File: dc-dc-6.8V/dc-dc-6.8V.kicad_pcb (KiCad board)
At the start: 2 copper layers, 32 x 37 mm, 23 parts, among them P1 1.8mm_16AWG, P2 1.8mm_16AWG, P3 1.8mm_16AWG, P4 1.8mm_16AWG, Q3 DOD4185, U2 LM25085MY/NOPB

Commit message: update
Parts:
- removed C10: 1nF, bio-robot:C_0603_1608Metric
- removed C11: 3.3nF, bio-robot:C_0603_1608Metric
- removed C12: 47uF, bio-robot:CAP_EEEFT1H470AP
- removed D2: STPS20M100SG-TR, bio-robot:TO-263-2
- removed H5, H6, H7, H8: MountingHoleM3, MountingHole:MountingHole_3.2mm_M3_DIN965_Pad
- removed L2: 3.3uH, bio-robot:IND_MDA1050-3R3M
- removed Q3: DOD4185, bio-robot:DPAK-3_ONS
- removed R5: 10m, bio-robot:R_0805_2012Metric
- removed R8: 10k, bio-robot:R_0603_1608Metric
- removed R9: 2.26k, bio-robot:R_0603_1608Metric
- removed U2: LM25085MY/NOPB, bio-robot:MSOP8_PowerPad
- added C1: 22u_1206, bots:C_1206_3216Metric, F.Cu at (117.2, 71.2)
- added C2: 22u_1206, bots:C_1206_3216Metric, F.Cu at (114.8, 71.2)
- added C3: 22u_1206, bots:C_1206_3216Metric, F.Cu at (112.2, 71.2)
- added C4: 0.1u, bots:C_0603_1608Metric, F.Cu at (119.2, 72.0)
- added C5: 15nF, bio-robot:C_0603_1608Metric, F.Cu at (149.2, 123.6)
- added C6: 0.47u, bio-robot:C_0603_1608Metric, F.Cu at (152.5, 118.2)
- added H1: MountingHoleM3, bio-robot:MountingHole_3.2mm_M3_DIN965_Pad, F.Cu at (109.5, 60.0)
- added H2: MountingHoleM3, bio-robot:MountingHole_3.2mm_M3_DIN965_Pad, F.Cu at (139.5, 60.0)
- added H3: MountingHoleM3, bio-robot:MountingHole_3.2mm_M3_DIN965_Pad, F.Cu at (109.5, 85.0)
- added H4: MountingHoleM3, bio-robot:MountingHole_3.2mm_M3_DIN965_Pad, F.Cu at (139.5, 85.0)
- added L1: 1.8uH, bio-robot:IND_XAL7070_COC, F.Cu at (131.0, 100.0)
- added Q1: SVD5865NLT4G, bots:DPAK-3_ONS, F.Cu at (127.8, 110.9)
- added Q2: SVD5865NLT4G, bots:DPAK-3_ONS, F.Cu at (136.7, 110.9)
- added R1: 137k, bio-robot:R_0603_1608Metric, F.Cu at (121.2, 104.6)
- added R2: 806R, bots:R_0603_1608Metric, F.Cu at (121.2, 107.1)
- added U1: LM3150MHX_NOPB, bio-robot:SOP65P640X110-15N, F.Cu at (124.8, 74.5)
- C7: value 22u_1206 -> 2.2u; footprint bots:C_1206_3216Metric -> bio-robot:C_0603_1608Metric
- C8: value 22u_1206 -> 180pF; footprint bots:C_1206_3216Metric -> bio-robot:C_0603_1608Metric
- C9: value 0.47u -> 82uF; footprint bio-robot:C_0603_1608Metric -> bio-robot:CAP_10SVPC120MV
- R3: value 113k -> 9.76k; footprint bio-robot:R_0603_1608Metric -> bots:R_0603_1608Metric; moved to F.Cu
- R4: value 4.12k -> 102k; footprint bio-robot:R_0603_1608Metric -> bots:R_0603_1608Metric; moved to F.Cu
- moved R4 62.9 mm to (168.8, 109.2), turned to 0 degrees
- moved R3 57.8 mm to (149.2, 126.1), turned to 0 degrees
- moved P3 37.5 mm to (156.2, 63.2), turned to 90 degrees
- moved P4 37.2 mm to (154.0, 74.5), turned to 0 degrees
- moved C9 24.8 mm to (99.8, 90.8)
- moved C8 18.5 mm to (112.2, 94.1), turned to 0 degrees
- moved P1 17.3 mm to (95.2, 68.0), turned to 90 degrees
- moved P2 15.1 mm to (98.0, 76.5), turned to 180 degrees
- moved C7 9.39 mm to (122.5, 71.0), turned to 0 degrees
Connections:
- C7 pad 1: VCC -> /CVCC
- C8 pad 1: VCC -> +6.8V
- C8 pad 2: GND -> /FB
- C9 pad 1: VCC -> +6.8V
- C9 pad 2: /CVCC -> GND
- R3 pad 1: VCC -> /FB
- R3 pad 2: /RT -> GND
- R4 pad 1: /ADJ -> +6.8V
- R4 pad 2: VCC -> /FB
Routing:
- net /FB1: track 6.86 -> 0.00 mm
- net /ADJ: track 4.73 -> 0.00 mm, vias 1 -> 0
- net /RT: track 4.29 -> 0.00 mm, vias 1 -> 0
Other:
- board size 32 x 37 mm -> 37 x 32 mm

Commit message: update
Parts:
- C1, C2, C3: footprint bots:C_1206_3216Metric -> bio-robot:C_1206_3216Metric
- Q1, Q2: footprint bots:DPAK-3_ONS -> bio-robot:SOIC-8_3.9x4.9mm_P1.27mm
- moved C6 51.1 mm to (129.3, 72.8), turned to 180 degrees
- moved Q1 46.9 mm to (124.0, 64.2), turned to 180 degrees
- moved C5 46.5 mm to (126.0, 83.2), turned to 180 degrees
- moved R3 44.8 mm to (128.2, 86.5), turned to 180 degrees
- moved R4 44.0 mm to (131.2, 86.5), turned to 180 degrees
- moved Q2 42.2 mm to (124.0, 70.8)
- moved C9 36.6 mm to (133.5, 76.6), turned to -90 degrees
- moved R2 32.8 mm to (128.2, 75.1), turned to 90 degrees
- moved L1 32.5 mm to (132.6, 67.5), turned to 180 degrees
- moved R1 24.0 mm to (129.1, 82.0), turned to 90 degrees
- moved C8 21.0 mm to (131.2, 85.0), turned to 180 degrees
- moved P3 18.5 mm to (140.2, 72.5)
- moved P1 14.6 mm to (109.8, 66.5)
- moved P4 14.3 mm to (140.2, 78.5)
- moved P2 12.4 mm to (109.8, 72.5)
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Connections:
- net Net-(U1-ILIM) renamed /ILIM
- net Net-(U1-SS) renamed /SS
- Q1 pad 1: /HG -> /SW
- Q1 pad 2: VCC -> /SW
- Q2 pad 1: /LG -> GND
- Q2 pad 2: /SW -> GND
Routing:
- net +6.8V: track 0.00 -> 16.4 mm, vias 0 -> 2
- net /HG: track 0.00 -> 14.0 mm
- net /FB: track 0.00 -> 12.8 mm
- net /BST: track 0.00 -> 9.15 mm, vias 0 -> 2
- net /LG: track 0.00 -> 3.45 mm
- net /SW: track 0.00 -> 3.32 mm
- net /SS: track 0.00 -> 3.12 mm
- net /RON: track 0.00 -> 3.07 mm
- net VCC: track 0.00 -> 2.97 mm, vias 0 -> 20
- net /ILIM: track 0.00 -> 2.35 mm
- net GND: track 0.00 -> 1.15 mm, vias 0 -> 35
- added copper zone on F.Cu, net +6.8V
- added copper zone on F.Cu, net /CVCC
- added copper zone on F.Cu, net /SW
- added copper zone on F.Cu, net GND
- added copper zone on In1.Cu, net GND
- added copper zone on F.Cu, net VCC
- added copper zone on In2.Cu, net VCC
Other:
- copper layers 2 -> 4

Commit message: board files
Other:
- board text added: "6.8V Custom DC-DC MECH 540 / EECE 571M Marine Robotics Group 3: Quiet Bio-inspired Propulsion System Designed By: Henry Bryant Printed on: March 24th, 2026"
- board text added: "Designed for 16-14AWG 10A Current"
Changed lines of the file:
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@@
 		(layer "Edge.Cuts")
+	)
+	(gr_text "Designed for 16-14AWG \n10A Current"
+		(at 115.75 60.25 0)
+		(layer "F.SilkS")
+		(effects
+			(font
+				(size 1 1)
+				(thickness 0.1)
+			)
+			(justify left bottom)
+		)
 	)
 	(gr_text "6.8V"
@@
 		)
 	)
+	(gr_text "6.8V Custom DC-DC\nMECH 540 / EECE 571M Marine Robotics\nGroup 3: Quiet Bio-inspired Propulsion System\nDesigned By: Henry Bryant\nPrinted on: March 24th, 2026"
+		(at 138 62.75 35)
+		(layer "B.SilkS")
+		(effects
+			(font
+				(size 1 1)
+				(thickness 0.1)
+			)
+			(justify left bottom mirror)
+		)
+	)

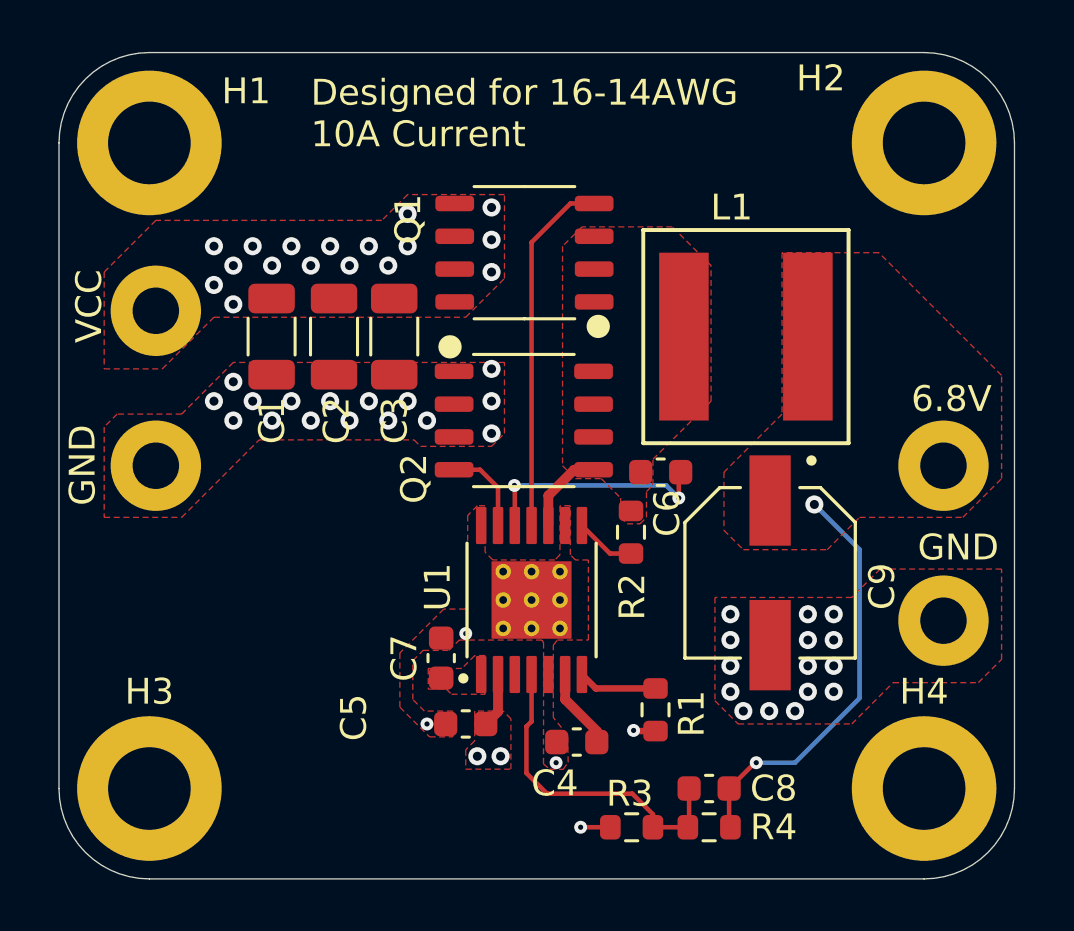
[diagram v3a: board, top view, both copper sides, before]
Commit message: 5V 5A version
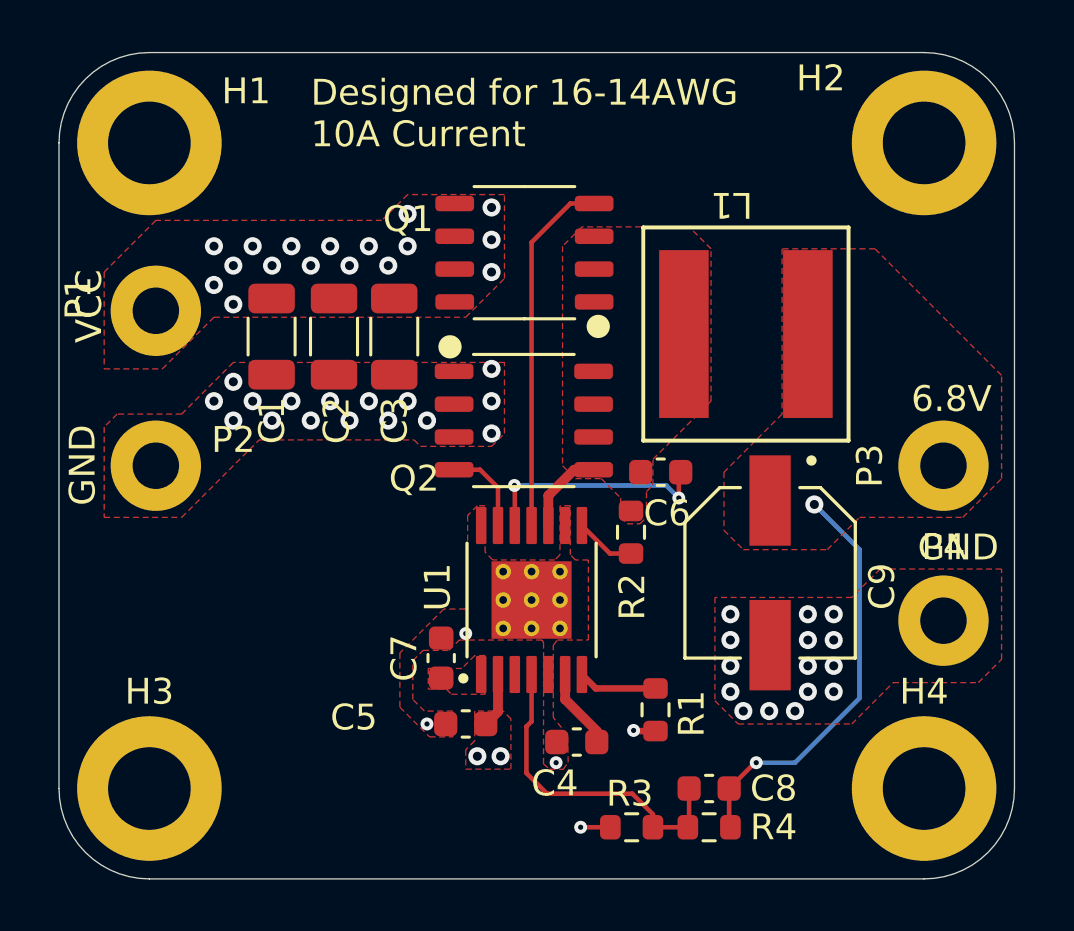
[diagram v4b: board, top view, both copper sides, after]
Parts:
- moved L1 0.10 mm to (132.6, 67.4)

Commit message: ordered
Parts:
- Q1, Q2: value SVD5865NLT4G -> AO4354
- R3: value 9.76k -> 10k; footprint bots:R_0603_1608Metric -> bio-robot:R_0603_1608Metric
- R4: value 102k -> 100k
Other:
- board text added: "6.8V Custom DC-DC MECH 540 / EECE 571M Marine Robotics Group 3: Quiet Bio-inspired Propulsion System Designed By: Henry Bryant Printed on: March 26th, 2026"
- board text removed: "6.8V Custom DC-DC MECH 540 / EECE 571M Marine Robotics Group 3: Quiet Bio-inspired Propulsion System Designed By: Henry Bryant Printed on: March 24th, 2026"
